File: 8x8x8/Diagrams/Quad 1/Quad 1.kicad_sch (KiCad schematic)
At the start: 87 parts

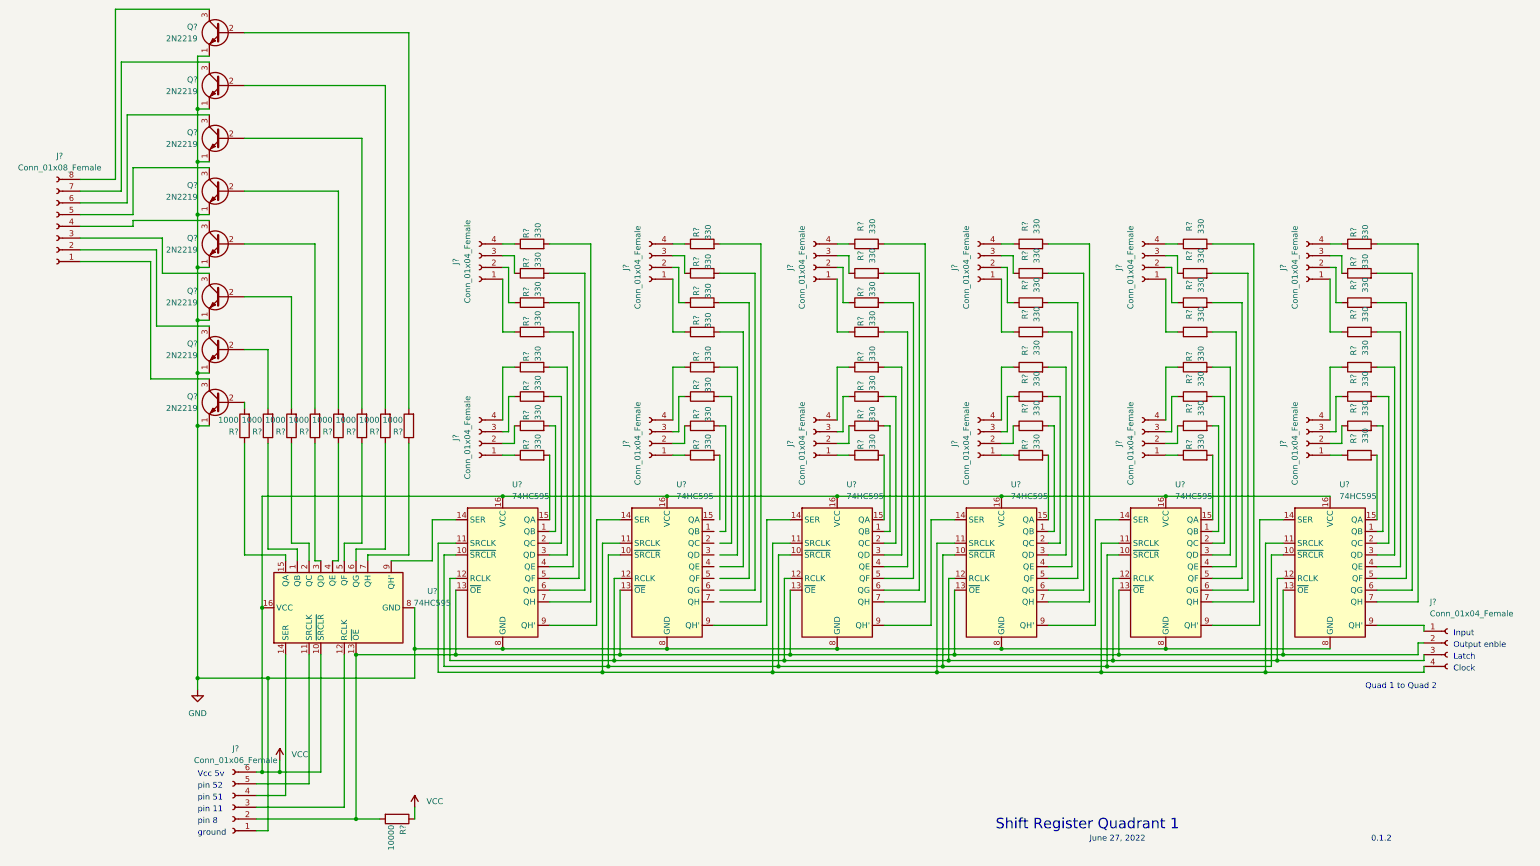
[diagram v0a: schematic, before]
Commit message: fixed diamgram quad 1 wiring
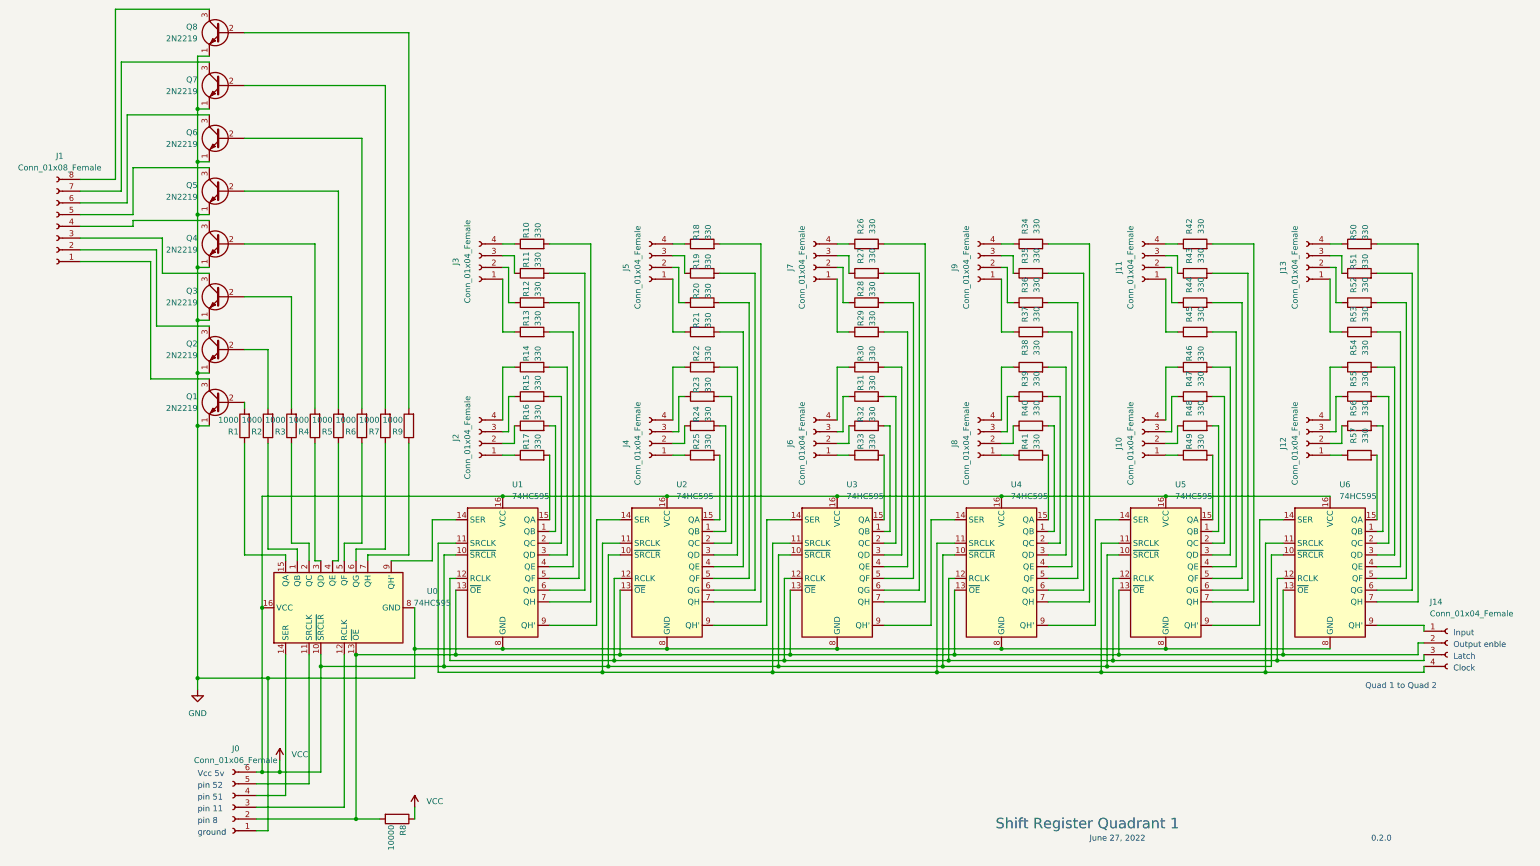
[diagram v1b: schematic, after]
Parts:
- gave numbers to parts that had none: 87
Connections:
- net VCC: now also U1.10 (~{SRCLR}), U2.10 (~{SRCLR}), U3.10 (~{SRCLR}), U4.10 (~{SRCLR}), U5.10 (~{SRCLR}), U6.10 (~{SRCLR})
- net at U2.1 (QB): now also R24.2
- net at U2.15 (QA): now also R25.2
- net at U2.2 (QC): now also R23.2
- net at U2.3 (QD): now also R22.2
- net at U2.4 (QE): now also R21.2
- net at U2.5 (QF): now also R20.2
- net at U2.6 (QG): now also R19.2
- net at U2.7 (QH): now also R18.2
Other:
- note added: "0.2.0"
- note removed: "0.1.2"

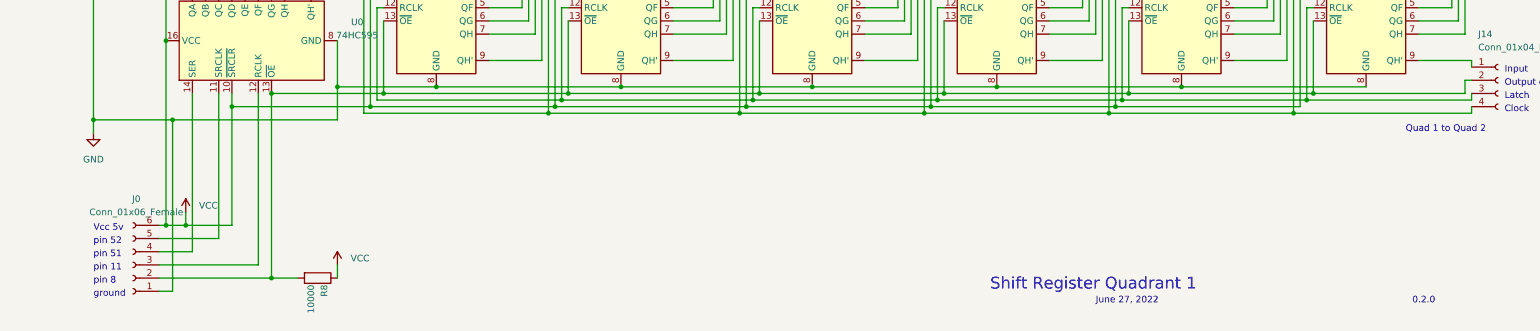
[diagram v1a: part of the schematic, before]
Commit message: connected latch and clock wires in diagram
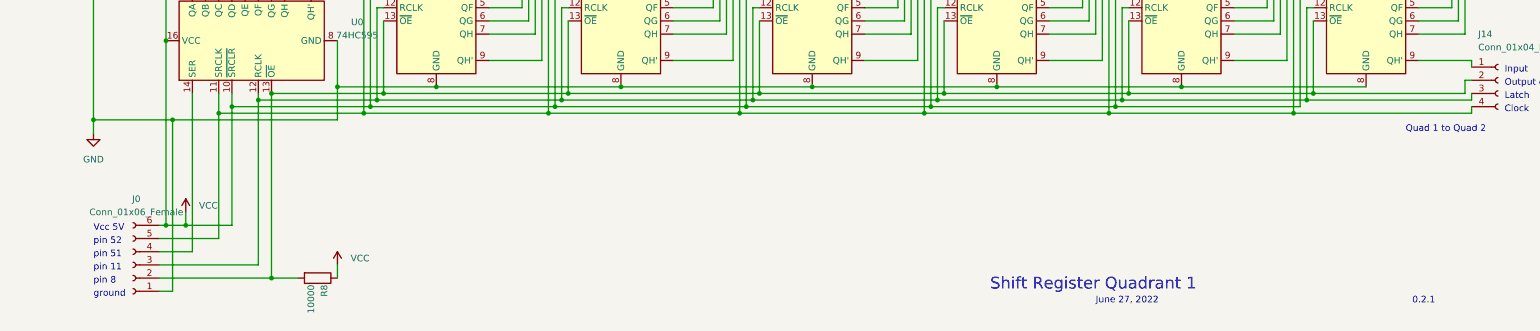
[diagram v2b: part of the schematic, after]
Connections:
- net at J14.4 (Pin_4), U1.11 (SRCLK), U2.11 (SRCLK)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: now also J0.5 (Pin_5), U0.11 (SRCLK)
- net at J14.3 (Pin_3), U1.12 (RCLK), U2.12 (RCLK)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: now also J0.3 (Pin_3), U0.12 (RCLK)
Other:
- note added: "0.2.1"
- note added: "Vcc 5V"
- note removed: "0.2.0"
- note removed: "Vcc 5v"
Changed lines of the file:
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@@
   (junction (at 176.53 154.94) (diameter 0) (color 0 0 0 0)
   )
+  (junction (at 45.72 154.94) (diameter 0) (color 0 0 0 0)
+  )
   (junction (at 80.01 119.38) (diameter 0) (color 0 0 0 0)
   )
@@
   (junction (at 173.99 157.48) (diameter 0) (color 0 0 0 0)
   )
+  (junction (at 66.04 157.48) (diameter 0) (color 0 0 0 0)
+  )
+  (junction (at 38.1 157.48) (diameter 0) (color 0 0 0 0)
+  )
   (junction (at 209.55 157.48) (diameter 0) (color 0 0 0 0)
   )
@@
   (junction (at 48.26 153.67) (diameter 0) (color 0 0 0 0)
   )
+  (junction (at 68.58 154.94) (diameter 0) (color 0 0 0 0)
+  )
   (junction (at 31.75 179.07) (diameter 0) (color 0 0 0 0)
   )
@@
     (stroke (width 0) (type default) (color 0 0 0 0))
   )
+  (wire (pts (xy 38.1 157.48) (xy 38.1 181.61))
+    (stroke (width 0) (type default) (color 0 0 0 0))
+  )
   (wire (pts (xy 224.79 77.47) (xy 226.06 77.47))
     (stroke (width 0) (type default) (color 0 0 0 0))
@@
     (stroke (width 0) (type default) (color 0 0 0 0))
   )
-  (wire (pts (xy 38.1 153.67) (xy 38.1 181.61))
+  (wire (pts (xy 38.1 153.67) (xy 38.1 157.48))
     (stroke (width 0) (type default) (color 0 0 0 0))
   )
@@
     (stroke (width 0) (type default) (color 0 0 0 0))
   )
-  (wire (pts (xy 45.72 153.67) (xy 45.72 186.69))
+  (wire (pts (xy 45.72 153.67) (xy 45.72 154.94))
     (stroke (width 0) (type default) (color 0 0 0 0))
   )
@@
     (stroke (width 0) (type default) (color 0 0 0 0))
   )
+  (wire (pts (xy 38.1 157.48) (xy 66.04 157.48))
+    (stroke (width 0) (type default) (color 0 0 0 0))
+  )
   (wire (pts (xy 162.56 147.32) (xy 172.72 147.32))
     (stroke (width 0) (type default) (color 0 0 0 0))
@@
     (stroke (width 0) (type default) (color 0 0 0 0))
   )
+  (wire (pts (xy 45.72 154.94) (xy 45.72 186.69))
+    (stroke (width 0) (type default) (color 0 0 0 0))
+  )
   (wire (pts (xy 236.22 97.79) (xy 233.68 97.79))
     (stroke (width 0) (type default) (color 0 0 0 0))
@@
   )
   (wire (pts (xy 130.81 91.44) (xy 130.81 132.08))
+    (stroke (width 0) (type default) (color 0 0 0 0))
+  )
+  (wire (pts (xy 45.72 154.94) (xy 68.58 154.94))
     (stroke (width 0) (type default) (color 0 0 0 0))
   )
@@
     (effects (font (size 1.27 1.27)) (justify left bottom))
   )
-  (text "0.2.0" (at 267.97 194.31 0)
+  (text "0.2.1" (at 267.97 194.31 0)
     (effects (font (size 1.27 1.27)) (justify left bottom))
   )
@@
     (effects (font (size 1.27 1.27)) (justify left bottom))
   )
-  (text "Vcc 5v" (at 13.97 180.34 0)
+  (text "Vcc 5V" (at 13.97 180.34 0)
     (effects (font (size 1.27 1.27)) (justify left bottom))
   )

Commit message: Finished quad 2-3
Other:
- note added: "Output"
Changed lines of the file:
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@@
     (effects (font (size 2.27 2.27)) (justify left bottom))
   )
+  (text "Output" (at 285.75 138.43 0)
+    (effects (font (size 1.27 1.27)) (justify left bottom))
+  )
   (text "pin 52\n" (at 13.97 182.88 0)
+    (effects (font (size 1.27 1.27)) (justify left bottom))
+  )
+  (text "Output" (at 217.17 78.74 0)
+    (effects (font (size 1.27 1.27)) (justify left bottom))
+  )
+  (text "Output" (at -12.7 45.72 0)
+    (effects (font (size 1.27 1.27)) (justify left bottom))
+  )
+  (text "Output" (at 110.49 100.33 0)
+    (effects (font (size 1.27 1.27)) (justify left bottom))
+  )
+  (text "Output" (at 73.66 77.47 0)
+    (effects (font (size 1.27 1.27)) (justify left bottom))
+  )
+  (text "Output" (at 146.05 77.47 0)
     (effects (font (size 1.27 1.27)) (justify left bottom))
   )
@@
     (effects (font (size 1.27 1.27)) (justify left bottom))
   )
+  (text "Output" (at 110.49 77.47 0)
+    (effects (font (size 1.27 1.27)) (justify left bottom))
+  )
+  (text "Output" (at 252.73 78.74 0)
+    (effects (font (size 1.27 1.27)) (justify left bottom))
+  )
   (text "June 27, 2022" (at 207.01 194.31 0)
+    (effects (font (size 1.27 1.27)) (justify left bottom))
+  )
+  (text "Output" (at 146.05 100.33 0)
     (effects (font (size 1.27 1.27)) (justify left bottom))
   )
@@
     (effects (font (size 1.27 1.27)) (justify left bottom))
   )
+  (text "Output" (at 181.61 77.47 0)
+    (effects (font (size 1.27 1.27)) (justify left bottom))
+  )
+  (text "Input" (at 29.21 196.85 0)
+    (effects (font (size 1.27 1.27)) (justify left bottom))
+  )
+  (text "Output" (at 252.73 100.33 0)
+    (effects (font (size 1.27 1.27)) (justify left bottom))
+  )
   (text "Output enble" (at 285.75 152.4 0)
+    (effects (font (size 1.27 1.27)) (justify left bottom))
+  )
+  (text "Output" (at 73.66 100.33 0)
     (effects (font (size 1.27 1.27)) (justify left bottom))
   )
@@
     (effects (font (size 1.27 1.27)) (justify left bottom))
   )
+  (text "Output" (at 181.61 100.33 0)
+    (effects (font (size 1.27 1.27)) (justify left bottom))
+  )
+  (text "Output" (at 217.17 100.33 0)
+    (effects (font (size 1.27 1.27)) (justify left bottom))
+  )

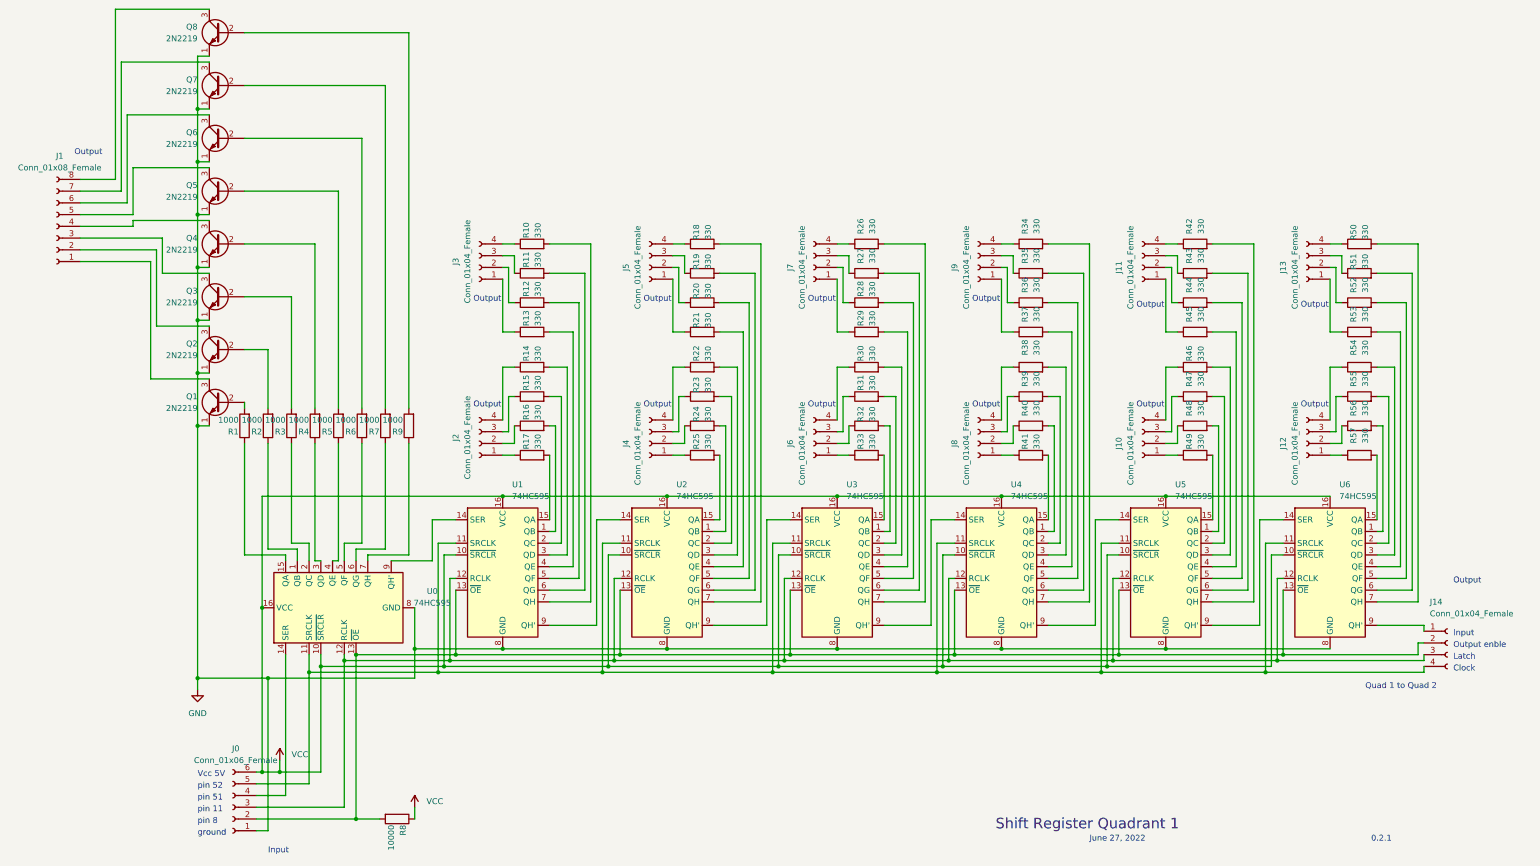
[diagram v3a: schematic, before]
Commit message: revised quad 1 diagram
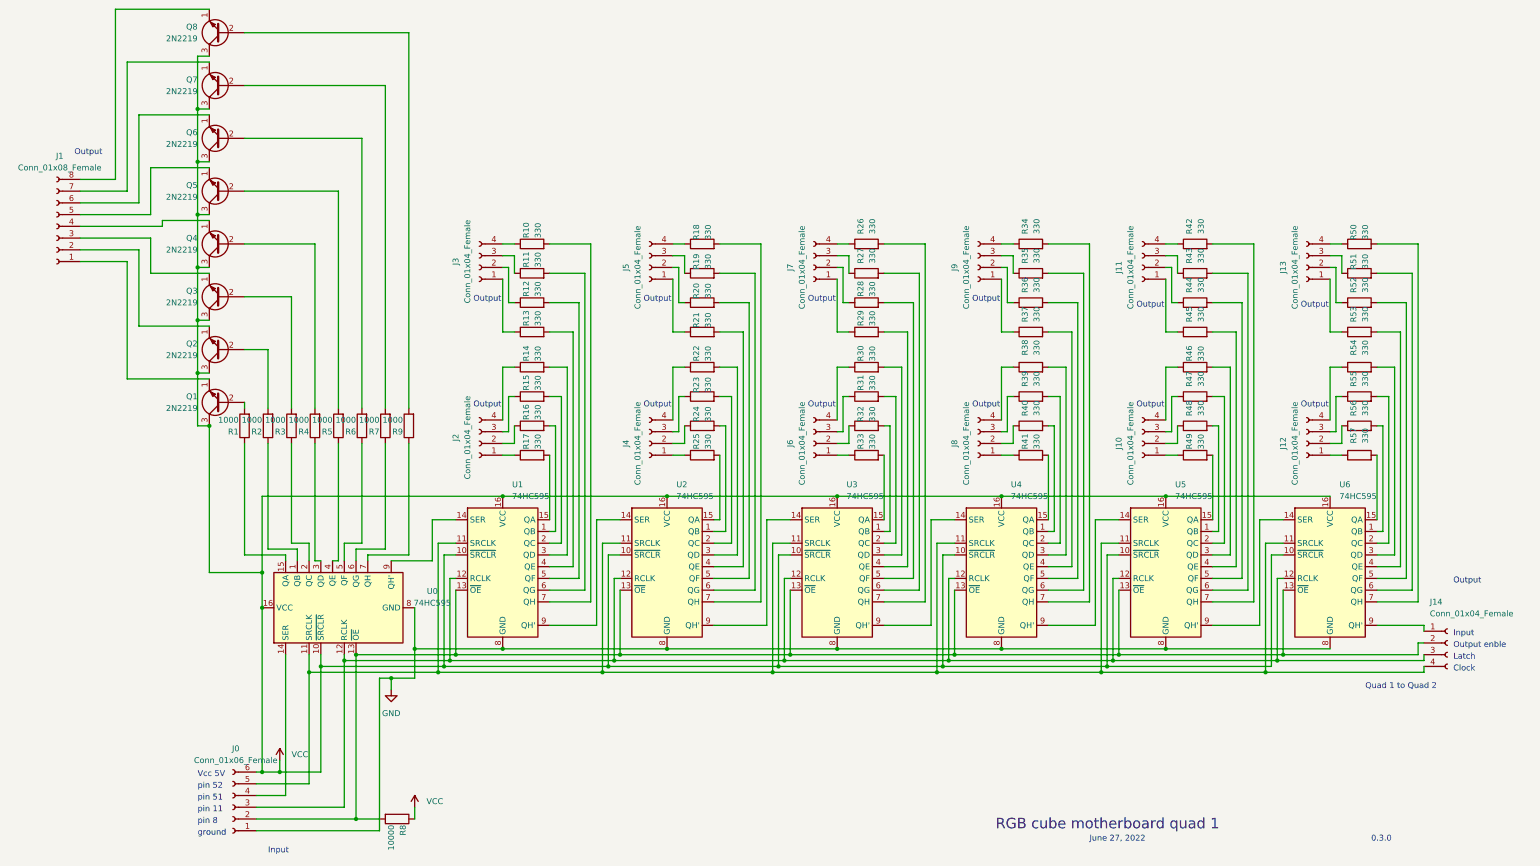
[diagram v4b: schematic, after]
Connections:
- net GND: no longer Q1.1 (E), Q2.1 (E), Q3.1 (E), Q4.1 (E), Q5.1 (E), Q6.1 (E), Q7.1 (E), Q8.1 (E)
- net VCC: now also Q1.3 (C), Q2.3 (C), Q3.3 (C), Q4.3 (C), Q5.3 (C), Q6.3 (C), Q7.3 (C), Q8.3 (C)
- net at J1.1 (Pin_1): now also Q1.1 (E); no longer Q1.3 (C)
- net at J1.2 (Pin_2): now also Q2.1 (E); no longer Q2.3 (C)
- net at J1.3 (Pin_3): now also Q3.1 (E); no longer Q3.3 (C)
- net at J1.4 (Pin_4): now also Q4.1 (E); no longer Q4.3 (C)
- net at J1.5 (Pin_5): now also Q5.1 (E); no longer Q5.3 (C)
- net at J1.6 (Pin_6): now also Q6.1 (E); no longer Q6.3 (C)
- net at J1.7 (Pin_7): now also Q7.1 (E); no longer Q7.3 (C)
- net at J1.8 (Pin_8): now also Q8.1 (E); no longer Q8.3 (C)
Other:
- note added: "0.3.0"
- note added: "RGB cube motherboard quad 1"
- note removed: "0.2.1"
- note removed: "Shift Register Quadrant 1"
- moved on the sheet: Q1, Q2, Q3, Q4, Q5, Q6, Q7, Q8

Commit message: finish general layout for pcb
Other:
- note added: "RGB cube Driver quad 1"
- note removed: "RGB cube motherboard quad 1"
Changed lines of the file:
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@@
     (effects (font (size 1.27 1.27)) (justify left bottom))
   )
-  (text "RGB cube motherboard quad 1" (at 186.69 191.77 0)
+  (text "RGB cube Driver quad 1" (at 186.69 191.77 0)
     (effects (font (size 2.27 2.27)) (justify left bottom))
   )
